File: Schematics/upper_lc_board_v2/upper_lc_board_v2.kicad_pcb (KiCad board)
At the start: 2 copper layers, 69.5 x 60 mm, 119 parts, among them J1 USB_C_Female_USB2_Small, J2 Stack Male Edge Connector, J3 SOL_CONN, J4 SOL_CONN, J5 HALL-1, J7 PT1, J8 PT1, Q1 2N7002, Q2 AO3400A, Q3 AO3400A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

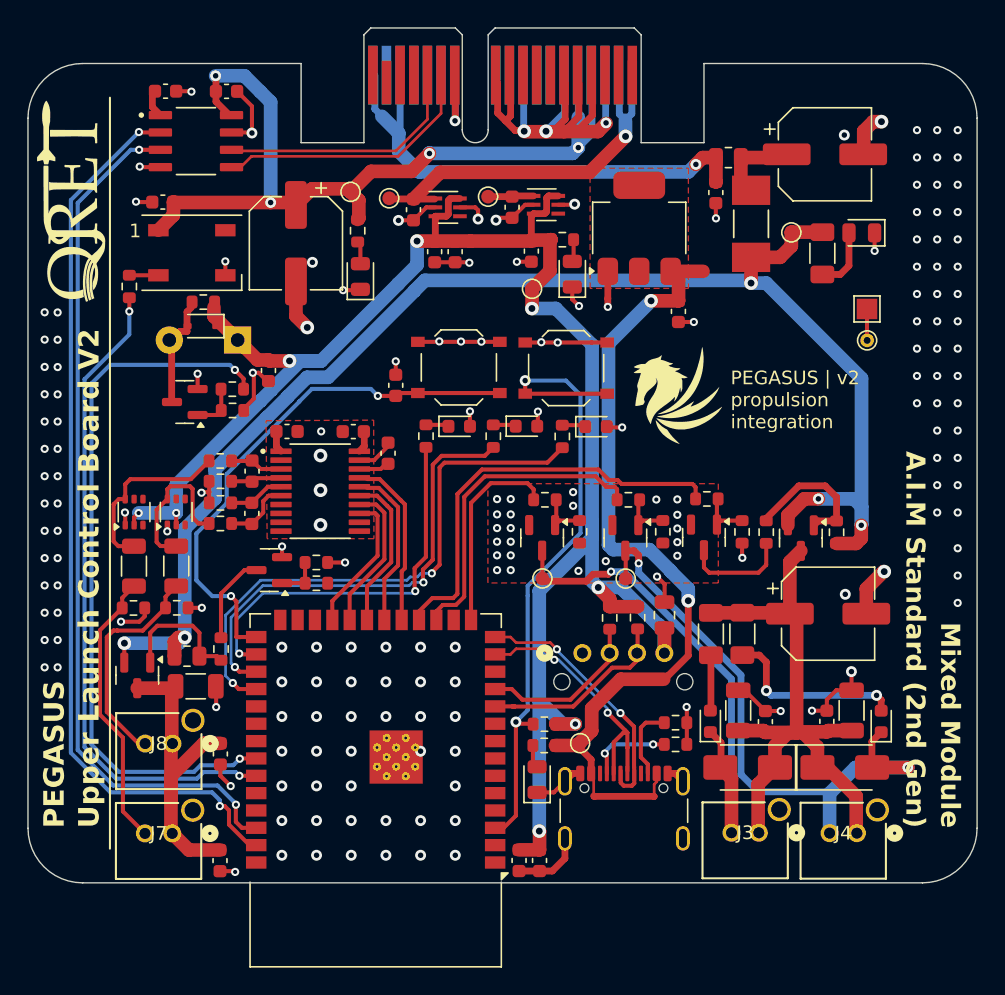
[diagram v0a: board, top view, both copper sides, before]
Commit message: add additional LEDs
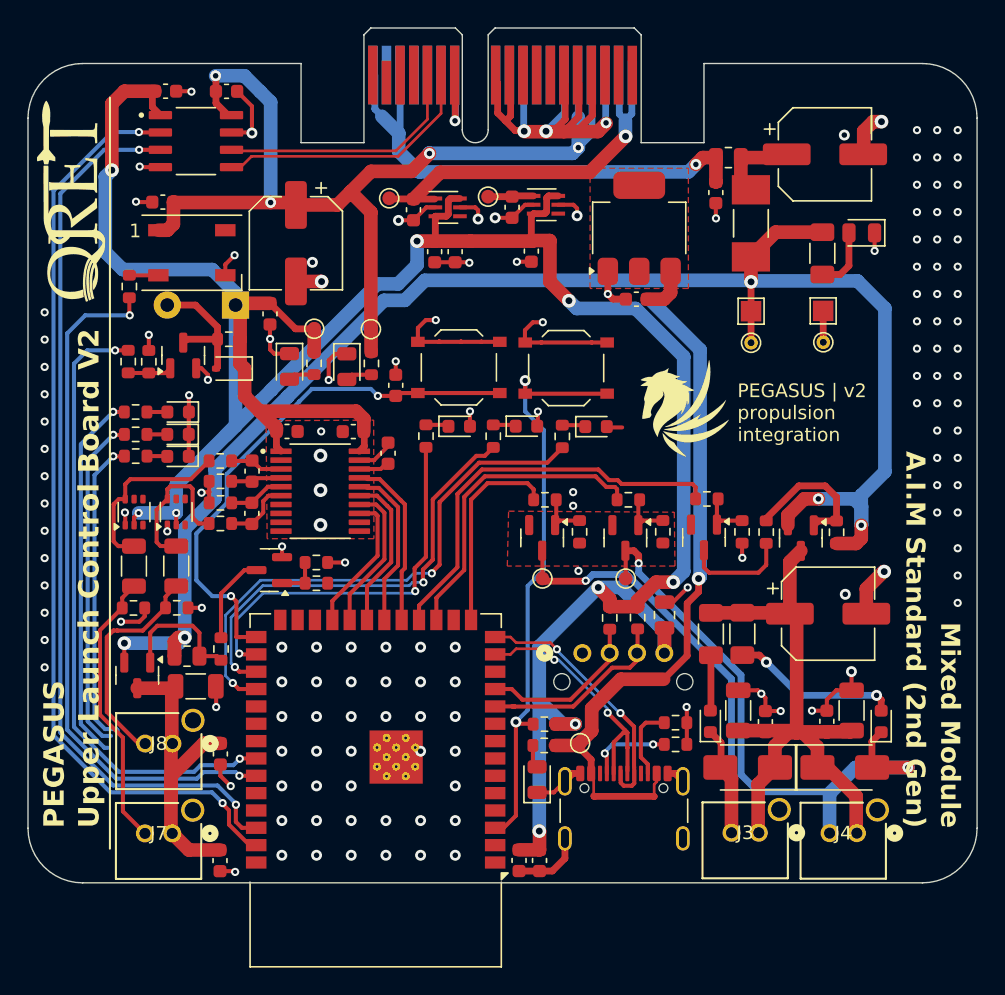
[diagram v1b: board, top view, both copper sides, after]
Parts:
- added D16: LED, LED_SMD:LED_0603_1608Metric, F.Cu at (119.0, 85.5)
- added D17: LED, LED_SMD:LED_0603_1608Metric, F.Cu at (119.0, 87.2)
- added D18: LED, LED_SMD:LED_0603_1608Metric, F.Cu at (119.0, 88.8)
- added R26: 150, Resistor_SMD:R_0603_1608Metric, F.Cu at (115.9, 85.5)
- added R40: 150, Resistor_SMD:R_0603_1608Metric, F.Cu at (115.9, 87.2)
- added R41: 150, Resistor_SMD:R_0603_1608Metric, F.Cu at (115.9, 88.8)
- added TP11: 24V-TP-H, TestPoint:TestPoint_THTPad_D1.0mm_Drill0.5mm, F.Cu at (160.9, 80.5)
- TP3: value 24V-TP -> 24V-TP-P; footprint TestPoint:TestPoint_Pad_D1.0mm -> TestPoint:TestPoint_Pad_1.5x1.5mm
- moved D5 21.8 mm to (127.1, 82.2), turned to -90 degrees
- moved R7 20.3 mm to (128.9, 82.0), turned to 90 degrees
- moved TP2 16.2 mm to (128.9, 79.4)
- moved TP4 10.2 mm to (133.1, 79.5)
- moved R9 9.77 mm to (133.1, 82.0)
- moved R27 7.89 mm to (115.3, 81.8), turned to 90 degrees
- moved R28 7.09 mm to (116.8, 81.8), turned to -90 degrees
- moved D7 6.67 mm to (131.3, 82.2), turned to -90 degrees
- moved TP3 6.48 mm to (160.9, 78.1)
- moved C23 4.15 mm to (125.7, 78.3)
- moved D15 3.74 mm to (122.8, 82.3)
- moved Q4 3.41 mm to (119.4, 81.4), turned to 90 degrees
- moved R29 3.30 mm to (122.7, 80.2)
- moved TP5 3.21 mm to (166.2, 78.1)
- moved TP7 3.21 mm to (166.2, 80.4)
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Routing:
- net +3V3: track 142.5 -> 198.1 mm, vias 8 -> 9
- net PT1_LED: track 0.00 -> 27.4 mm, vias 0 -> 1
- net PT2_LED: track 0.00 -> 24.7 mm, vias 0 -> 1
- net HALL_LED: track 0.00 -> 22.7 mm, vias 0 -> 1
- net +5V: track 63.3 -> 73.6 mm
- net GND: track 158.6 -> 168.2 mm, vias 191 -> 155
- net +24V: track 107.7 -> 117.0 mm
- net BUZZ_IN: track 52.6 -> 46.1 mm
- net 5V_USB: track 61.6 -> 55.2 mm, vias 2 -> 1
- net /ESP32-S3 Breakout Circuitry/ESP32_EN: track 47.5 -> 43.5 mm
- net /ESP32-S3 Breakout Circuitry/GPIO_42: track 48.1 -> 51.1 mm
- net Net-(BZ1--): track 7.84 -> 10.1 mm
- net /ESP32-S3 Breakout Circuitry/GPIO_02: track 64.1 -> 66.3 mm
- net /ESP32-S3 Breakout Circuitry/GPIO_01: track 66.4 -> 68.4 mm
- net Net-(D16-A): track 0.00 -> 1.50 mm
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
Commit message: add silkscreen
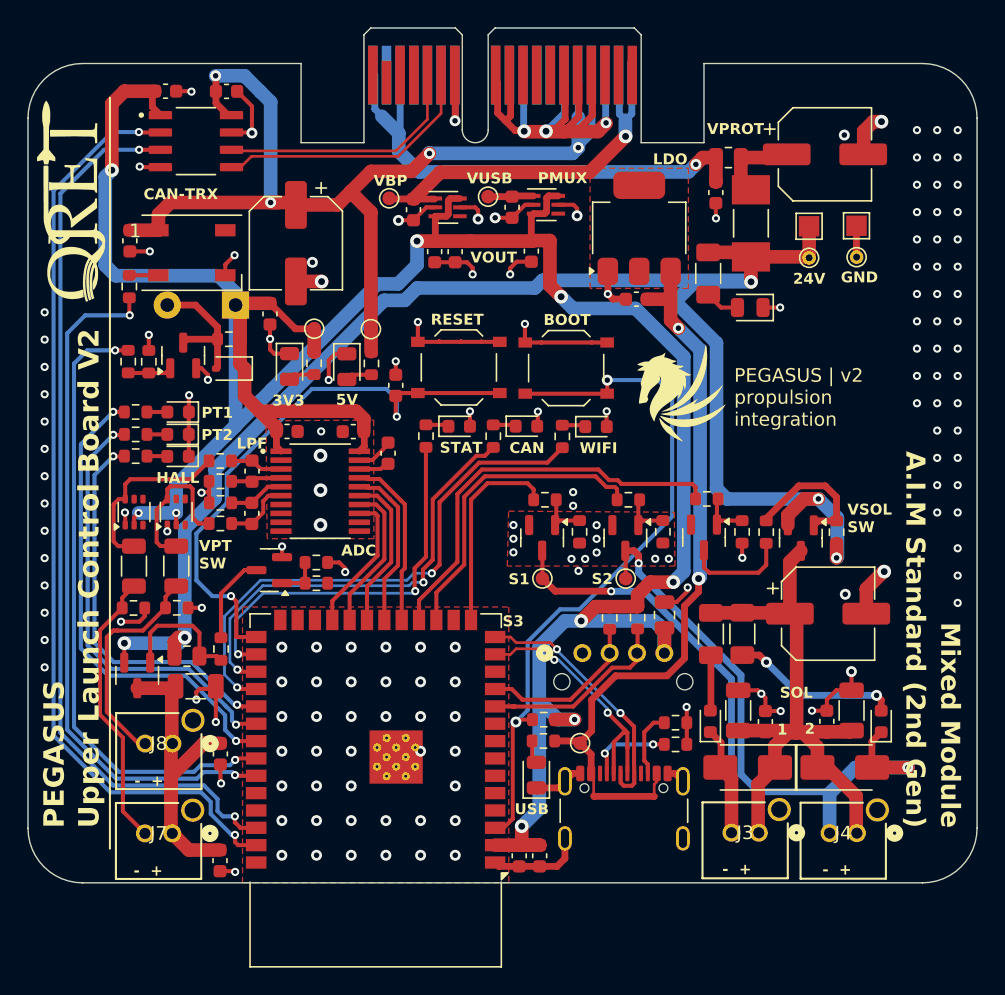
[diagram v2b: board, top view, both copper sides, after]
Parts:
- moved D6 9.83 mm to (160.9, 77.9)
- moved R8 8.49 mm to (157.8, 75.4)
- moved TP11 7.53 mm to (165.2, 74.2)
- moved TP3 7.53 mm to (165.2, 71.9)
- moved TP5 6.70 mm to (168.7, 71.9)
- moved TP7 6.70 mm to (168.7, 74.2)
- moved C27 3.72 mm to (115.5, 73.0), turned to -90 degrees
- moved G*** 1.15 mm to (155.7, 84.5)
- moved C2 0.34 mm to (144.0, 118.0)
- moved C3 0.34 mm to (145.5, 118.0)
- moved D8 0.33 mm to (145.2, 112.1)
- moved R1 0.33 mm to (145.8, 108.0)
- moved R10 0.33 mm to (145.7, 109.6)
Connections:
- U1 pad 31: /ESP32-S3 Breakout Circuitry/GPIO_38 -> HALL_LED
- U1 pad 32: /ESP32-S3 Breakout Circuitry/GPIO_39 -> PT2_LED
- U1 pad 33: /ESP32-S3 Breakout Circuitry/GPIO_40 -> PT1_LED
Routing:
- net /ESP32-S3 Breakout Circuitry/ESP32_EN: track 43.5 -> 51.8 mm
- net PT1_LED: track 27.4 -> 35.5 mm, vias 1 -> 2
- net PT2_LED: track 24.7 -> 32.3 mm, vias 1 -> 2
- net HALL_LED: track 22.7 -> 28.8 mm, vias 1 -> 2
- net GND: track 168.2 -> 172.4 mm, vias 155 -> 167
- net /ESP32-S3 Breakout Circuitry/ESP32_IO0: track 39.5 -> 42.5 mm
- net +3V3: track 198.1 -> 200.8 mm
- net +5V: track 73.6 -> 75.9 mm
- net Net-(D6-A): track 4.63 -> 2.53 mm
- net +24V: track 117.0 -> 116.4 mm
- net Net-(J1-CC2): track 5.44 -> 4.89 mm
- net 5V_USB: track 55.2 -> 55.1 mm, vias 1 -> 2
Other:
- copper layers 2 -> 4
- board text added: "- +"
- board text added: "1"
- board text added: "2"
- board text added: "24V"
- board text added: "3V3"
- board text added: "5V"
- board text added: "ADC"
- board text added: "BOOT"
- board text added: "CAN"
- board text added: "CAN-TRX"
- board text added: "GND"
- board text added: "HALL"
- board text added: "LDO"
- board text added: "LPF"
- board text added: "PMUX"
- board text added: "PT1"
- board text added: "PT2"
- board text added: "RESET"
- board text added: "S1"
- board text added: "S2"
- board text added: "S3"
- board text added: "SOL"
- board text added: "STAT"
- board text added: "USB"
- board text added: "VBP"
- board text added: "VOUT"
- board text added: "VPROT"
- board text added: "VPT SW"
- board text added: "VSOL SW"
- board text added: "VUSB"
- board text added: "WIFI"

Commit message: gnd pour
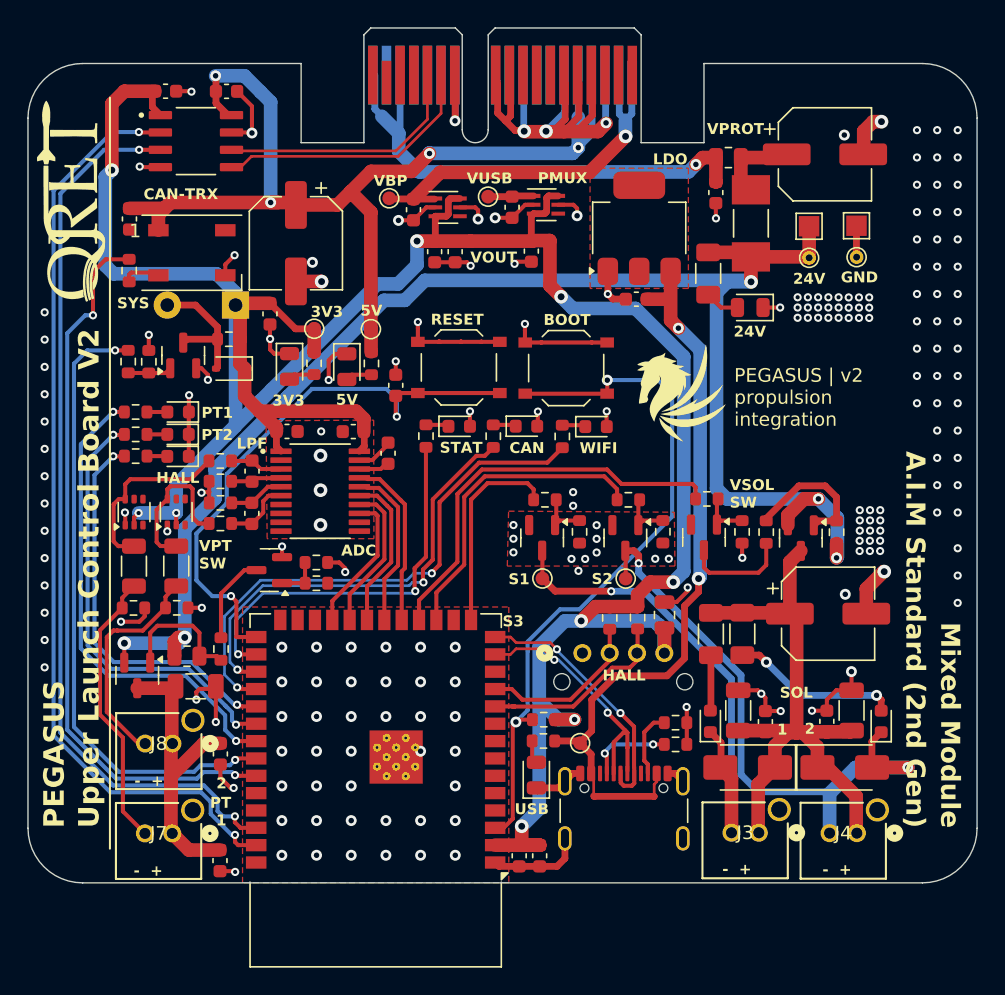
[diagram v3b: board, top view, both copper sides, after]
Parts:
- moved C27 1.60 mm to (115.4, 71.4)
- moved R30 1.17 mm to (115.4, 75.2), turned to -90 degrees
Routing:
- net +24V: track 116.4 -> 112.4 mm
- net /ESP32-S3 Breakout Circuitry/GPIO_42: track 51.4 -> 53.6 mm
- net GND: track 172.4 -> 170.2 mm, vias 167 -> 205
- net +5V: track 75.9 -> 77.0 mm
- net Net-(D4-DOUT): track 2.13 -> 2.81 mm
- added copper zone on In1.Cu, net GND
- added copper zone on In2.Cu, net GND
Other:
- board text added: "+ SD SC -"
- board text added: "PT"
- board text added: "SYS"
- board text added: "bzz"

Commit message: small adjusmetns
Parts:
- moved R35 0.25 mm to (119.1, 96.8)
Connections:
- U1 pad 24: /ESP32-S3 Breakout Circuitry/GPIO_47 -> VPT-SW
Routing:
- net +3V3: track 200.8 -> 214.8 mm, vias 9 -> 11
- net GND: track 170.2 -> 175.6 mm, vias 205 -> 204
- net VPT-SW: track 0.00 -> 3.08 mm
- net Net-(D14A-K3A4): track 11.3 -> 12.5 mm

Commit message: s
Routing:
- net /ESP32-S3 Breakout Circuitry/USB_N: track 19.2 -> 18.0 mm
- net +3V3: track 214.8 -> 213.7 mm
- net +5V: vias 4 -> 3
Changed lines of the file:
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@@
 	)
 	(segment
-		(start 123.19 86.52)
-		(end 122.44 87.27)
-		(width 1)
-		(layer "B.Cu")
-		(net 3)
-	)
-	(segment
 		(start 133.567056 76.142944)
 		(end 125.81 83.9)
@@
 	(segment
 		(start 123.25 102)
-		(end 123.59 102)
-		(width 0.3)
-		(layer "F.Cu")
-		(net 4)
-	)
-	(segment
-		(start 123.25 102)
 		(end 124.7 102)
 		(width 0.3)
@@
 	)
 	(via
-		(at 148.29 66.16)
-		(size 0.8)
-		(drill 0.4)
-		(layers "F.Cu" "B.Cu")
-		(net 5)
-	)
-	(via
 		(at 121.73 60.9)
 		(size 0.8)
@@
 	)
 	(segment
-		(start 143.61 107.09)
-		(end 143.6 107.08)
-		(width 0.3)
-		(layer "F.Cu")
-		(net 54)
-	)
-	(segment
-		(start 143.6 107.08)
-		(end 142.2 107.08)
-		(width 0.3)
-		(layer "F.Cu")
-		(net 54)
-	)
-	(segment
 		(start 147.92 107.09)
 		(end 143.61 107.09)
@@
 	)
 	(segment
-		(start 143.61 107.09)
-		(end 143.44 107.09)
-		(width 0.3)
-		(layer "F.Cu")
-		(net 54)
-	)
-	(segment
 		(start 150.77 104.24)
 		(end 147.92 107.09)
@@
 	)
 	(segment
+		(start 143.6 107.08)
+		(end 142.2 107.08)
+		(width 0.3)
+		(layer "F.Cu")
+		(net 54)
+	)
+	(segment
 		(start 152.07 104.24)
 		(end 150.77 104.24)
@@
 	)
 	(segment
+		(start 143.61 107.09)
+		(end 143.6 107.08)
+		(width 0.3)
+		(layer "F.Cu")
+		(net 54)
+	)
+	(segment
 		(start 114.94 114.76545)
 		(end 114.94 109.367106)
@@
 	)
 	(segment
-		(start 151.73 108.849239)
-		(end 151.88 108.999239)
-		(width 0.3)
-		(layer "F.Cu")
-		(net 75)
-	)
-	(segment
-		(start 151.89 110.095786)
-		(end 151.89 111.785)
+		(start 150.88 107.99)
+		(end 150.438578 107.548578)
 		(width 0.3)
 		(layer "F.Cu")
@@
 	)
 	(segment
-		(start 150.438578 107.548578)
-		(end 151.73 108.84)
-		(width 0.3)
-		(layer "F.Cu")
-		(net 75)
-	)
-	(segment
 		(start 146.53 103.67)
 		(end 145.72 102.86)
@@
 	)
 	(segment
-		(start 150.438578 107.541422)
-		(end 150.438578 107.548578)
+		(start 151.89 110.72)
+		(end 151.89 111.785)
 		(width 0.3)
 		(layer "F.Cu")
@@
 	(segment
 		(start 150.88 109.71)
-		(end 151.590761 108.999239)
+		(end 151.89 110.72)
 		(width 0.3)
 		(layer "F.Cu")
@@
 	)
 	(segment
-		(start 151.88 110.085786)
-		(end 151.89 110.095786)
+		(start 150.438578 107.548578)
+		(end 150.438578 107.541422)
 		(width 0.3)
 		(layer "F.Cu")
@@
 	)
 	(segment
-		(start 151.88 108.999239)
-		(end 151.88 110.085786)
-		(width 0.3)
-		(layer "F.Cu")
-		(net 75)
-	)
-	(segment
-		(start 151.590761 108.999239)
-		(end 151.88 108.999239)
-		(width 0.3)
-		(layer "F.Cu")
-		(net 75)
-	)
-	(segment
-		(start 151.73 108.84)
-		(end 151.73 108.849239)
+		(start 150.88 109.71)
+		(end 150.88 107.99)
 		(width 0.3)
 		(layer "F.Cu")

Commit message: review work
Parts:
- removed D16, D17, D18: LED, LED_SMD:LED_0603_1608Metric
- removed Q1: 2N7002, Package_TO_SOT_SMD:SOT-23
- removed R11, R13: 10k, Resistor_SMD:R_0603_1608Metric
- removed R12: 4.7k, Resistor_SMD:R_0603_1608Metric
- removed R14: 200, Resistor_SMD:R_0603_1608Metric
- removed R26, R40, R41: 150, Resistor_SMD:R_0603_1608Metric
- removed U6: DMP4065S-7, Package_TO_SOT_SMD:SOT-23
- added C1: 1uF, Capacitor_SMD:C_0603_1608Metric, F.Cu at (152.0, 81.0)
- moved TP6 5.92 mm to (140.3, 70.2)
- moved TP9 5.53 mm to (147.2, 70.1)
- moved U5 2.62 mm to (143.3, 70.5), turned to -90 degrees
- moved C11 2.39 mm to (138.6, 70.3)
- moved U4 2.27 mm to (136.4, 70.5), turned to -90 degrees
- moved C12 2.03 mm to (145.4, 70.3)
- moved G*** 1.25 mm to (156.2, 85.7)
- moved R19 0.07 mm to (152.0, 91.9)
- moved R17 0.05 mm to (145.9, 92.0)
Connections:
- C13 pad 1: VSOL -> +24V
- C18 pad 1: VSOL -> +24V
- C19 pad 1: VSOL -> +24V
- C20 pad 1: VSOL -> +24V
- C21 pad 1: VSOL -> +24V
- D11 pad 1: VSOL -> +24V
- D12 pad 1: VSOL -> +24V
- J3 pad 1: VSOL -> +24V
- J4 pad 1: VSOL -> +24V
- R15 pad 2: VSOL -> +24V
- R16 pad 2: VSOL -> +24V
- R2 pad 1: /ESP32-S3 Breakout Circuitry/GPIO_35 -> /ESP32-S3 Breakout Circuitry/GPIO_37
- R4 pad 1: /ESP32-S3 Breakout Circuitry/GPIO_37 -> /ESP32-S3 Breakout Circuitry/GPIO_35
- U1 pad 15: VALVE1_CTRL -> /ESP32-S3 Breakout Circuitry/GPIO_03
- U1 pad 17: VALVE2_CTRL -> VALVE1_CTRL
- U1 pad 18: VSOL-SW -> VALVE2_CTRL
- U1 pad 31: HALL_LED -> /ESP32-S3 Breakout Circuitry/GPIO_38
- U1 pad 32: PT2_LED -> /ESP32-S3 Breakout Circuitry/GPIO_39
- U1 pad 33: PT1_LED -> /ESP32-S3 Breakout Circuitry/GPIO_40
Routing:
- net VSOL: track 47.2 -> 0.00 mm
- net +24V: track 112.4 -> 150.5 mm, vias 5 -> 4
- net PT1_LED: track 35.5 -> 0.00 mm, vias 2 -> 0
- net PT2_LED: track 32.3 -> 0.00 mm, vias 2 -> 0
- net VSOL-SW: track 30.0 -> 0.00 mm
- net HALL_LED: track 28.8 -> 0.00 mm, vias 2 -> 0
- net Net-(U6-G): track 10.2 -> 0.00 mm
- net /ESP32-S3 Breakout Circuitry/GPIO_37: track 39.6 -> 30.2 mm
- net /Power Circuitry/3V3_USB: track 3.36 -> 11.7 mm
- net /ESP32-S3 Breakout Circuitry/GPIO_35: track 28.7 -> 37.0 mm
- net Net-(Q1-D): track 7.80 -> 0.00 mm
- net GND: track 175.6 -> 170.4 mm, vias 204 -> 300
- net Net-(Q1-G): track 3.88 -> 0.00 mm
- net /ESP32-S3 Breakout Circuitry/ESP32_EN: track 51.8 -> 54.5 mm
- net +3V3: track 213.7 -> 216.2 mm
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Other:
- board text added: "Upper Control Board V2"
- board text removed: "PT1"
- board text removed: "PT2"
- board text removed: "S3"
- board text removed: "Upper Launch Control Board V2"
- board text removed: "VSOL SW"
